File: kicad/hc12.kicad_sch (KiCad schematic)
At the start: 8 parts

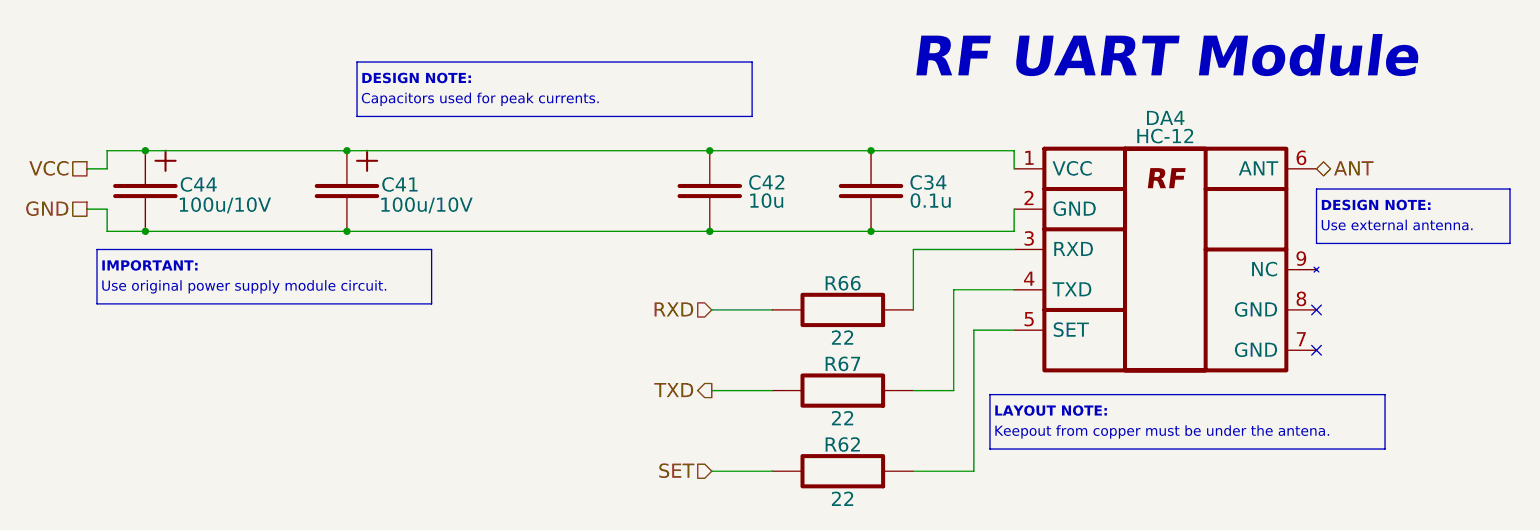
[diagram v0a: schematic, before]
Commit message: Reannotate schematic; Fix 5032 crystal footprint field; Update PCB with 5032 crystal
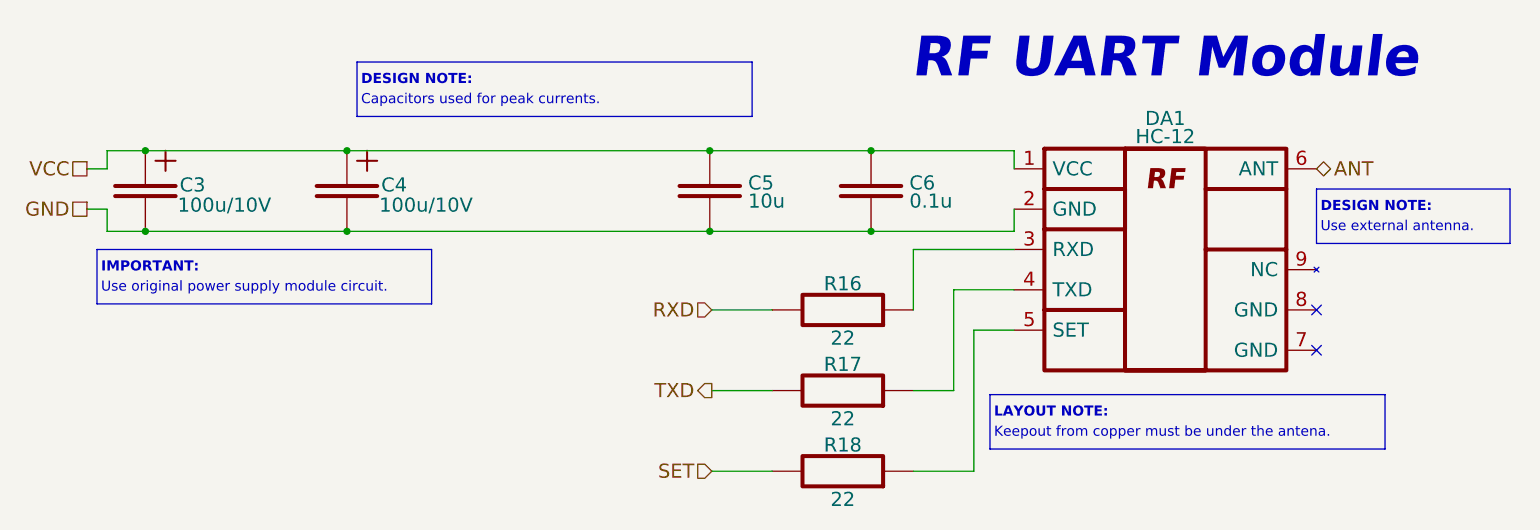
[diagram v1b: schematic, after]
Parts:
- renumbered C44 to C3, C41 to C4, C42 to C5, C34 to C6, DA4 to DA1, R66 to R16, R67 to R17, R62 to R18
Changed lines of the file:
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@@
   (symbol (lib_id "Resistors:R_RES") (at 161.036 122.174 180) (unit 1)
     (in_bom yes) (on_board yes)
-    (property "Reference" "R62" (id 0) (at 161.036 118.872 0)
+    (property "Reference" "R18" (id 0) (at 161.036 118.872 0)
       (effects (font (size 1.778 1.778)))
     )
@@
   (symbol (lib_id "Resistors:R_RES") (at 161.036 112.014 180) (unit 1)
     (in_bom yes) (on_board yes)
-    (property "Reference" "R67" (id 0) (at 161.036 108.712 0)
+    (property "Reference" "R17" (id 0) (at 161.036 108.712 0)
       (effects (font (size 1.778 1.778)))
     )
@@
   (symbol (lib_id "Capacitors:C_CAP") (at 144.272 86.868 270) (unit 1)
     (in_bom yes) (on_board yes)
-    (property "Reference" "C42" (id 0) (at 149.098 85.8521 90)
+    (property "Reference" "C5" (id 0) (at 149.098 85.8521 90)
       (effects (font (size 1.778 1.778)) (justify left))
     )
@@
   (symbol (lib_id "Resistors:R_RES") (at 161.036 101.854 180) (unit 1)
     (in_bom yes) (on_board yes)
-    (property "Reference" "R66" (id 0) (at 161.036 98.552 0)
+    (property "Reference" "R16" (id 0) (at 161.036 98.552 0)
       (effects (font (size 1.778 1.778)))
     )
@@
   (symbol (lib_id "Capacitors:C_CAP_PLUS") (at 73.152 86.868 270) (unit 1)
     (in_bom yes) (on_board yes)
-    (property "Reference" "C44" (id 0) (at 77.47 86.106 90)
+    (property "Reference" "C3" (id 0) (at 77.47 86.106 90)
       (effects (font (size 1.778 1.778)) (justify left))
     )
@@
   (symbol (lib_id "Capacitors:C_CAP_PLUS") (at 98.552 86.868 270) (unit 1)
     (in_bom yes) (on_board yes)
-    (property "Reference" "C41" (id 0) (at 102.87 86.106 90)
+    (property "Reference" "C4" (id 0) (at 102.87 86.106 90)
       (effects (font (size 1.778 1.778)) (justify left))
     )
@@
   (symbol (lib_id "Chips:HC-12") (at 201.676 81.534 0) (unit 1)
     (in_bom yes) (on_board yes)
-    (property "Reference" "DA4" (id 0) (at 201.676 77.724 0)
+    (property "Reference" "DA1" (id 0) (at 201.676 77.724 0)
       (effects (font (size 1.778 1.778)))
     )
@@
   (symbol (lib_id "Capacitors:C_CAP") (at 164.592 86.868 270) (unit 1)
     (in_bom yes) (on_board yes)
-    (property "Reference" "C34" (id 0) (at 169.418 85.8521 90)
+    (property "Reference" "C6" (id 0) (at 169.418 85.8521 90)
       (effects (font (size 1.778 1.778)) (justify left))
     )

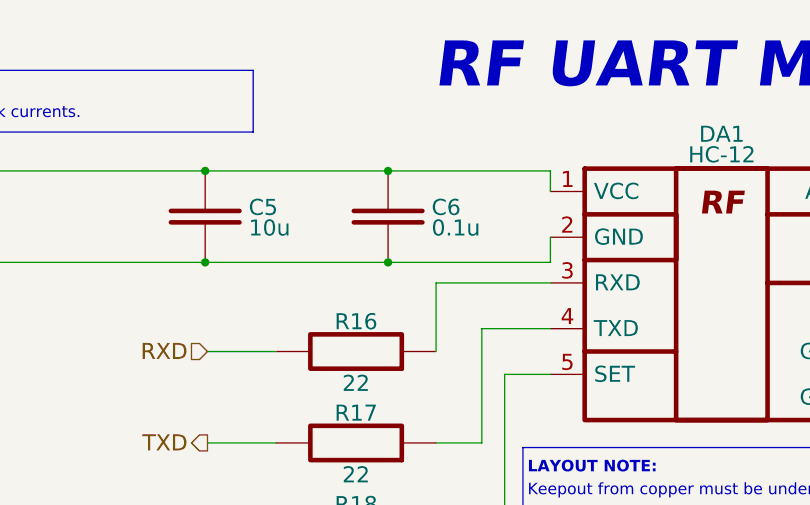
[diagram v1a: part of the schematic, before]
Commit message: Add voltage value to caps, update BOM, SCH, ASM
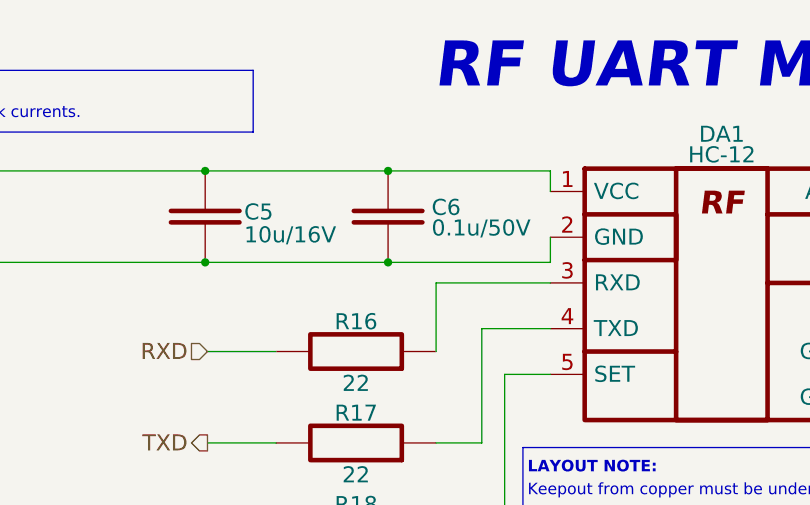
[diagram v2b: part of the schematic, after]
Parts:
- C5: value 10u -> 10u/16V; Case/Package (none) -> 1206; Tolerance (none) -> ±10%; Type (none) -> X7R
- C6: value 0.1u -> 0.1u/50V; Tolerance (none) -> ±10%; Type (none) -> X7R
- R16, R17, R18: Case/Package 0000 -> 0603; Tolerance ±% -> ±5%
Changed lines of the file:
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@@
     (effects (font (size 1.778 1.778)) (justify right))
   )
-  (symbol (lib_id "Resistors:R_RES") (at 161.036 122.174 180) (unit 1)
+  (symbol (lib_name "R_RES_1") (lib_id "Resistors:R_RES") (at 161.036 122.174 180) (unit 1)
     (in_bom yes) (on_board yes)
     (property "Reference" "R18" (id 0) (at 161.036 118.872 0)
@@
       (effects (font (size 1.778 1.778)))
     )
-    (property "Case/Package" "0000" (id 5) (at 161.036 115.824 0)
+    (property "Case/Package" "0603" (id 5) (at 161.036 115.824 0)
       (effects (font (size 1.27 1.27)) hide)
     )
@@
       (effects (font (size 1.27 1.27)) hide)
     )
-    (property "Tolerance" "±%" (id 7) (at 161.036 112.522 0)
-      (effects (font (size 1.27 1.27)) hide)
-    )
-    (pin "1")
-    (pin "2")
-  )
-  (symbol (lib_id "Resistors:R_RES") (at 161.036 112.014 180) (unit 1)
+    (property "Tolerance" "±5%" (id 7) (at 161.036 112.522 0)
+      (effects (font (size 1.27 1.27)) hide)
+    )
+    (property "Part Number" "" (id 8) (at 161.036 122.174 0))
+    (pin "1")
+    (pin "2")
+  )
+  (symbol (lib_name "R_RES_2") (lib_id "Resistors:R_RES") (at 161.036 112.014 180) (unit 1)
     (in_bom yes) (on_board yes)
     (property "Reference" "R17" (id 0) (at 161.036 108.712 0)
@@
       (effects (font (size 1.778 1.778)))
     )
-    (property "Case/Package" "0000" (id 5) (at 161.036 105.664 0)
+    (property "Case/Package" "0603" (id 5) (at 161.036 105.664 0)
       (effects (font (size 1.27 1.27)) hide)
     )
@@
       (effects (font (size 1.27 1.27)) hide)
     )
-    (property "Tolerance" "±%" (id 7) (at 161.036 102.362 0)
-      (effects (font (size 1.27 1.27)) hide)
-    )
-    (pin "1")
-    (pin "2")
-  )
-  (symbol (lib_id "Capacitors:C_CAP") (at 144.272 86.868 270) (unit 1)
-    (in_bom yes) (on_board yes)
-    (property "Reference" "C5" (id 0) (at 149.098 85.8521 90)
-      (effects (font (size 1.778 1.778)) (justify left))
-    )
-    (property "Value" "10u" (id 1) (at 149.098 88.1381 90)
+    (property "Tolerance" "±5%" (id 7) (at 161.036 102.362 0)
+      (effects (font (size 1.27 1.27)) hide)
+    )
+    (property "Part Number" "" (id 8) (at 161.036 112.014 0))
+    (pin "1")
+    (pin "2")
+  )
+  (symbol (lib_name "C_CAP_1") (lib_id "Capacitors:C_CAP") (at 144.272 86.868 270) (unit 1)
+    (in_bom yes) (on_board yes)
+    (property "Reference" "C5" (id 0) (at 148.59 86.36 90)
+      (effects (font (size 1.778 1.778)) (justify left))
+    )
+    (property "Value" "10u/16V" (id 1) (at 148.59 88.9 90)
       (effects (font (size 1.778 1.778)) (justify left))
     )
@@
       (effects (font (size 1.778 1.778)) hide)
     )
+    (property "Voltage" "" (id 5) (at 144.272 86.868 0)
+      (effects (font (size 1.27 1.27)) hide)
+    )
+    (property "Case/Package" "1206" (id 6) (at 144.272 86.868 0)
+      (effects (font (size 1.27 1.27)) hide)
+    )
+    (property "Type" "X7R" (id 7) (at 134.112 86.868 0)
+      (effects (font (size 1.27 1.27)) hide)
+    )
+    (property "Tolerance" "±10%" (id 8) (at 131.572 86.868 0)
+      (effects (font (size 1.27 1.27)) hide)
+    )
     (pin "1")
     (pin "2")
@@
       (effects (font (size 1.778 1.778)))
     )
-    (property "Case/Package" "0000" (id 5) (at 161.036 95.504 0)
+    (property "Case/Package" "0603" (id 5) (at 161.036 95.504 0)
       (effects (font (size 1.27 1.27)) hide)
     )
@@
       (effects (font (size 1.27 1.27)) hide)
     )
-    (property "Tolerance" "±%" (id 7) (at 161.036 92.202 0)
-      (effects (font (size 1.27 1.27)) hide)
-    )
+    (property "Tolerance" "±5%" (id 7) (at 161.036 92.202 0)
+      (effects (font (size 1.27 1.27)) hide)
+    )
+    (property "Part Number" "" (id 8) (at 161.036 101.854 0))
     (pin "1")
     (pin "2")
@@
       (effects (font (size 1.778 1.778)) (justify left))
     )
-    (property "Value" "0.1u" (id 1) (at 169.418 88.1381 90)
+    (property "Value" "0.1u/50V" (id 1) (at 169.418 88.1381 90)
       (effects (font (size 1.778 1.778)) (justify left))
     )
@@
       (effects (font (size 1.778 1.778)) hide)
     )
-    (pin "1")
+    (property "Voltage" "" (id 5) (at 164.592 86.868 0)
+      (effects (font (size 1.27 1.27)) hide)
+    )
+    (property "Case/Package" "" (id 6) (at 164.592 86.868 0)
+      (effects (font (size 1.27 1.27)) hide)
+    )
+    (property "Type" "X7R" (id 7) (at 154.432 86.868 0)
+      (effects (font (size 1.27 1.27)) hide)
+    )
+    (property "Tolerance" "±10%" (id 8) (at 151.892 86.868 0)
+      (effects (font (size 1.27 1.27)) hide)
+    )
+    (pin "1")

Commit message: Add wiring diagram; Add work ours (stage 2); refactor folders
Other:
- title: (none) -> RadioSens v1
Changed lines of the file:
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@@
 (kicad_sch (version 20211123) (generator eeschema)
   (paper "A4")
+  (title_block
+    (title "RadioSens v1")
+    (comment 2 "Electrical Circuit")
+  )
   (junction (at 144.272 91.948) (diameter 0) (color 0 0 0 0)
   )
